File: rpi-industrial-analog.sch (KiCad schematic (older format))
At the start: 68 parts, among them J101 CONN_01X04, J102 CONN_01X08, U101 MCP3424, U102 ICL7660S,A, U103 AD8220, U104 AD8220, U105 AD8220, U106 AD8220

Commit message: Layout complete
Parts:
- added LG101: 3ML_LOGO, 3ML_Footprint_Library:3ML_LOGO, symbol 3ML_LOGO
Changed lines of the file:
@@
+	1    0    0    -1
+$EndComp
+$Comp
+L 3ML_LOGO LG101
+U 1 1 58D9BA61
+P 10800 4450
+F 0 "LG101" H 10810 4590 60  0001 C CNN
+F 1 "3ML_LOGO" H 10800 4310 60  0001 C CNN
+F 2 "3ML_Footprint_Library:3ML_LOGO" H 10800 4450 60  0001 C CNN
+F 3 "X" H 10800 4450 60  0001 C CNN
+F 4 "X" H 10800 4450 60  0001 C CNN "MPN"
+F 5 "X" H 10800 4450 60  0001 C CNN "MFN"
+F 6 "X" H 10800 4450 60  0001 C CNN "Characteristics"
+F 7 "X" H 10800 4450 60  0001 C CNN "Description"
+F 8 "X" H 10800 4450 60  0001 C CNN "Package ID"
+F 9 "X" H 10800 4450 60  0001 C CNN "Source"
+F 10 "Y" H 10800 4450 60  0001 C CNN "Critical"
+F 11 "X" H 10800 4450 60  0001 C CNN "Notes"
+	1    10800 4450
 	1    0    0    -1
 $EndComp

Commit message: adding logos and mounting holes
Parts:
- added ACC101, ACC103, ACC104, ACC105: ACC_?, Mounting_Holes:MountingHole_3.2mm_M3_DIN965, symbol ACC_?
- added ACC102: ACC_?, Symbols:OSHW-Logo_5.7x6mm_SilkScreen, symbol ACC_?
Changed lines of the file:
@@
+	1    0    0    -1
+$EndComp
+$Comp
+L ACC_? ACC101
+U 1 1 58D9BFB7
+P 10800 4800
+F 0 "ACC101" H 10810 4940 60  0000 C CNN
+F 1 "ACC_?" H 10800 4660 60  0000 C CNN
+F 2 "Mounting_Holes:MountingHole_3.2mm_M3_DIN965" H 10800 4800 60  0001 C CNN
+F 3 "X" H 10800 4800 60  0001 C CNN
+F 4 "X" H 10800 4800 60  0001 C CNN "MPN"
+F 5 "X" H 10800 4800 60  0001 C CNN "MFN"
+F 6 "X" H 10800 4800 60  0001 C CNN "Characteristics"
+F 7 "Mounting Hole M3" H 10800 4800 60  0001 C CNN "Description"
+F 8 "X" H 10800 4800 60  0001 C CNN "Package ID"
+F 9 "X" H 10800 4800 60  0001 C CNN "Source"
+F 10 "Y" H 10800 4800 60  0001 C CNN "Critical"
+F 11 "X" H 10800 4800 60  0001 C CNN "Notes"
+	1    10800 4800
+	1    0    0    -1
+$EndComp
+$Comp
+L ACC_? ACC103
+U 1 1 58D9C882
+P 11150 4800
+F 0 "ACC103" H 11160 4940 60  0000 C CNN
+F 1 "ACC_?" H 11150 4660 60  0000 C CNN
+F 2 "Mounting_Holes:MountingHole_3.2mm_M3_DIN965" H 11150 4800 60  0001 C CNN
+F 3 "X" H 11150 4800 60  0001 C CNN
+F 4 "X" H 11150 4800 60  0001 C CNN "MPN"
+F 5 "X" H 11150 4800 60  0001 C CNN "MFN"
+F 6 "X" H 11150 4800 60  0001 C CNN "Characteristics"
+F 7 "Mounting Hole M3" H 11150 4800 60  0001 C CNN "Description"
+F 8 "X" H 11150 4800 60  0001 C CNN "Package ID"
+F 9 "X" H 11150 4800 60  0001 C CNN "Source"
+F 10 "Y" H 11150 4800 60  0001 C CNN "Critical"
+F 11 "X" H 11150 4800 60  0001 C CNN "Notes"
+	1    11150 4800
+	1    0    0    -1
+$EndComp
+$Comp
+L ACC_? ACC104
+U 1 1 58D9C980
+P 11500 4800
+F 0 "ACC104" H 11510 4940 60  0000 C CNN
+F 1 "ACC_?" H 11500 4660 60  0000 C CNN
+F 2 "Mounting_Holes:MountingHole_3.2mm_M3_DIN965" H 11500 4800 60  0001 C CNN
+F 3 "X" H 11500 4800 60  0001 C CNN
+F 4 "X" H 11500 4800 60  0001 C CNN "MPN"
+F 5 "X" H 11500 4800 60  0001 C CNN "MFN"
+F 6 "X" H 11500 4800 60  0001 C CNN "Characteristics"
+F 7 "Mounting Hole M3" H 11500 4800 60  0001 C CNN "Description"
+F 8 "X" H 11500 4800 60  0001 C CNN "Package ID"
+F 9 "X" H 11500 4800 60  0001 C CNN "Source"
+F 10 "Y" H 11500 4800 60  0001 C CNN "Critical"
+F 11 "X" H 11500 4800 60  0001 C CNN "Notes"
+	1    11500 4800
+	1    0    0    -1
+$EndComp
+$Comp
+L ACC_? ACC105
+U 1 1 58D9CA7D
+P 11850 4800
+F 0 "ACC105" H 11860 4940 60  0000 C CNN
+F 1 "ACC_?" H 11850 4660 60  0000 C CNN
+F 2 "Mounting_Holes:MountingHole_3.2mm_M3_DIN965" H 11850 4800 60  0001 C CNN
+F 3 "X" H 11850 4800 60  0001 C CNN
+F 4 "X" H 11850 4800 60  0001 C CNN "MPN"
+F 5 "X" H 11850 4800 60  0001 C CNN "MFN"
+F 6 "X" H 11850 4800 60  0001 C CNN "Characteristics"
+F 7 "Mounting Hole M3" H 11850 4800 60  0001 C CNN "Description"
+F 8 "X" H 11850 4800 60  0001 C CNN "Package ID"
+F 9 "X" H 11850 4800 60  0001 C CNN "Source"
+F 10 "Y" H 11850 4800 60  0001 C CNN "Critical"
+F 11 "X" H 11850 4800 60  0001 C CNN "Notes"
+	1    11850 4800
+	1    0    0    -1
+$EndComp
+$Comp
+L ACC_? ACC102
+U 1 1 58D9CBD3
+P 10800 5250
+F 0 "ACC102" H 10810 5390 60  0000 C CNN
+F 1 "ACC_?" H 10800 5110 60  0000 C CNN
+F 2 "Symbols:OSHW-Logo_5.7x6mm_SilkScreen" H 10800 5250 60  0001 C CNN
+F 3 "X" H 10800 5250 60  0001 C CNN
+F 4 "X" H 10800 5250 60  0001 C CNN "MPN"
+F 5 "X" H 10800 5250 60  0001 C CNN "MFN"
+F 6 "X" H 10800 5250 60  0001 C CNN "Characteristics"
+F 7 "Mounting Hole M3" H 10800 5250 60  0001 C CNN "Description"
+F 8 "X" H 10800 5250 60  0001 C CNN "Package ID"
+F 9 "X" H 10800 5250 60  0001 C CNN "Source"
+F 10 "Y" H 10800 5250 60  0001 C CNN "Critical"
+F 11 "X" H 10800 5250 60  0001 C CNN "Notes"
+	1    10800 5250
 	1    0    0    -1
 $EndComp

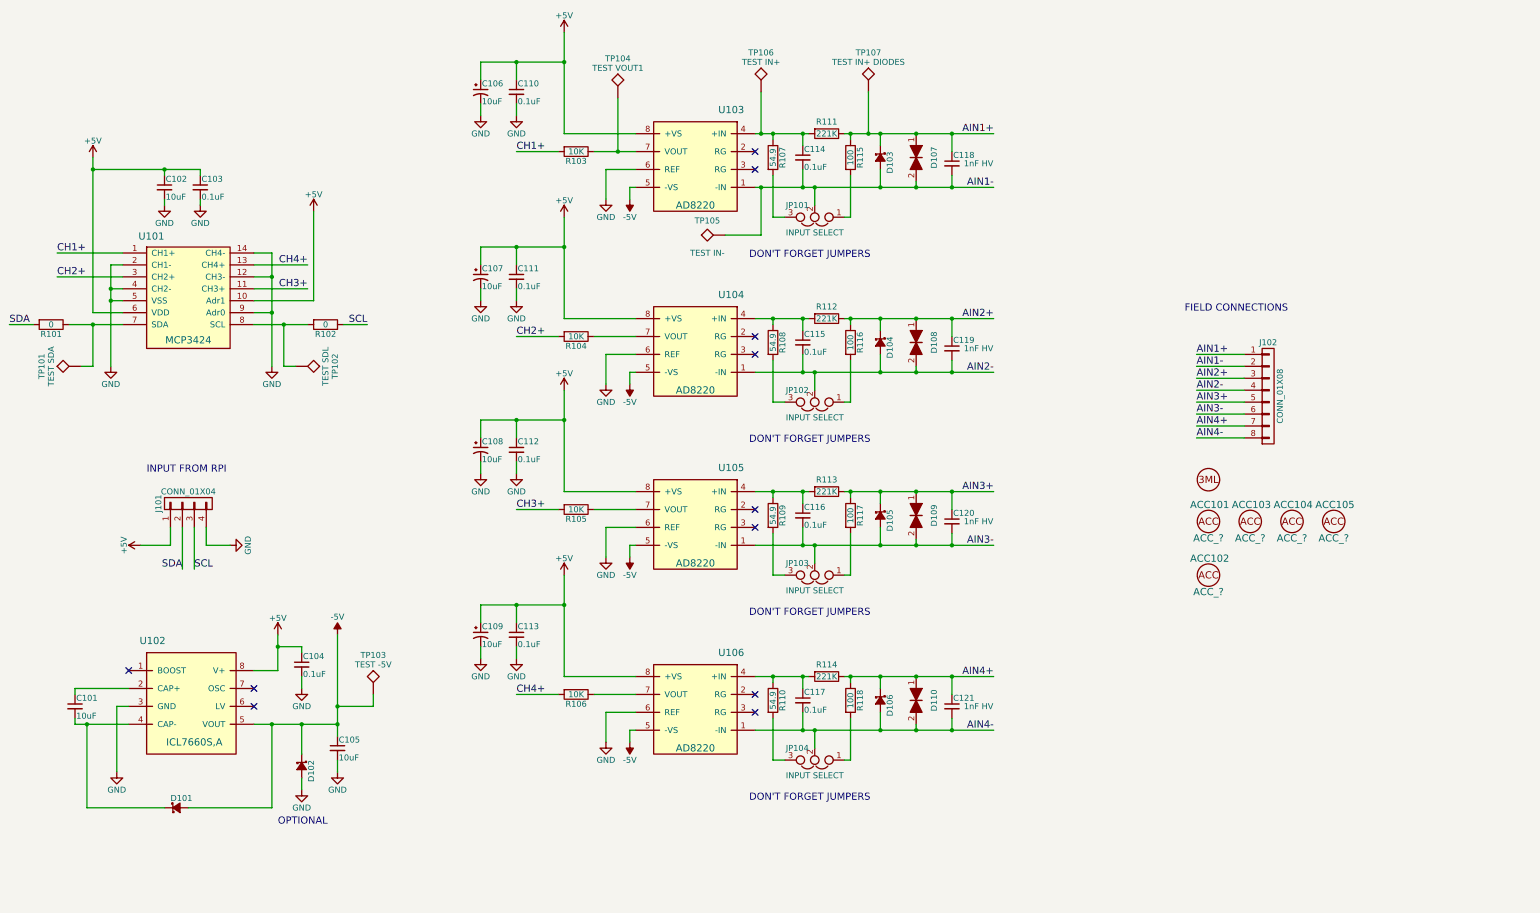
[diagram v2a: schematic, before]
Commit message: revised board for production and added 1M caps so that this thing works
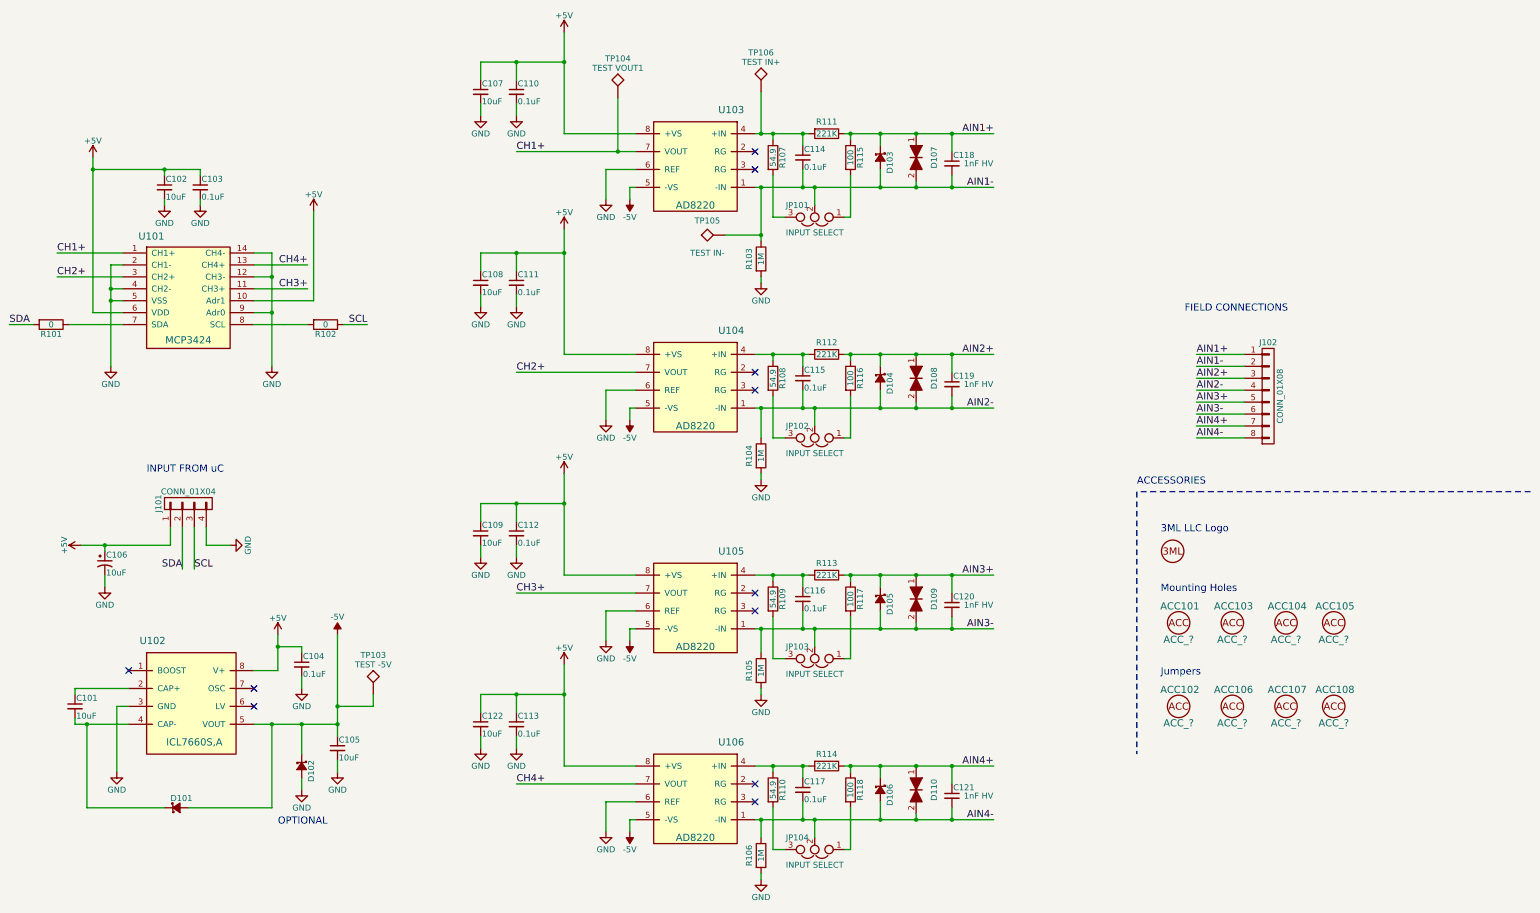
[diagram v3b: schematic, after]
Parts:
- removed C107, C108, C109: 10uF, 3ML_Footprint_Library:C_0805_POL, symbol CP1_Small
- removed TP101: TEST SDA, 3ML_Footprint_Library:Keystone_5000_Test_Point_Mini, symbol TEST
- removed TP102: TEST SDL, 3ML_Footprint_Library:Keystone_5000_Test_Point_Mini, symbol TEST
- removed TP107: TEST IN+ DIODES, 3ML_Footprint_Library:Keystone_5000_Test_Point_Mini, symbol TEST
- added ACC106, ACC107, ACC108: ACC_?, X, symbol ACC_?
- added C107, C108, C109, C122: 10uF, Capacitors_SMD:C_0805, symbol C_Small
- ACC102: footprint Symbols:OSHW-Logo_5.7x6mm_SilkScreen -> X; Description Mounting Hole M3 -> CONN JUMPER SHORTING 1.27MM GOLD; MFN X -> Sullins Connector Solutions; MPN X -> NPB02SVAN-RC; Populate (none) -> 1; Source X -> Digikey
- C106: footprint 3ML_Footprint_Library:C_0805_POL -> Capacitors_Tantalum_SMD:CP_Tantalum_Case-A_EIA-3216-18_Reflow; Description CAP TANT POLY 10UF 10V SMD -> F931A106KAA; MPN F381A106MMAAH1 -> (none); Package ID 0805 -> 1206 (3216 Metric); Populate (none) -> 1
- R103, R104, R105, R106: value 10K -> 1M; Characteristics X -> Value; Description RES SMD 10K OHM 1% 1/4W 0805 -> Value; MFN Stackpole Electronics -> Value; MPN RNCP0805FTD10K0 -> (none); Package ID 0805 -> Value; Populate (none) -> 1
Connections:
- net +5V: now also C107.1, C108.1, C109.1, C122.1
- net AIN1-: now also R103.1
- net AIN2-: now also R104.1
- net AIN3-: now also R105.1
- net AIN4-: now also R106.1
- net CH1+: now also TP104.1, U103.7 (VOUT); no longer R103.2
- net CH2+: now also U104.7 (VOUT); no longer R104.2
- net CH3+: now also U105.7 (VOUT); no longer R105.2
- net CH4+: now also U106.7 (VOUT); no longer R106.2
- net GND: now also R103.2, R104.2, R105.2, R106.2, C107.2, C108.2, C109.2, C122.2
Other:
- note added: "3ML LLC Logo"
- note added: "ACCESSORIES"
- note added: "INPUT FROM uC"
- note added: "Jumpers"
- note added: "Mounting Holes"
- note removed: "DON'T FORGET JUMPERS"
- note removed: "INPUT FROM RPI"
- moved on the sheet: ACC101, ACC103, ACC104, ACC105, C111, C112, C113, C115, C116, C117, C119, C120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

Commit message: adding gerbers, fixing DRC, adding overvoltage diodes to MCP inputs
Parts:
- added D111, D112, D113, D114: D_Schottky_Small_ALT, Diodes_SMD:D_SOD-323, symbol D_Schottky_Small_ALT
- J101: MFN Value -> Harwin; MPN Value -> M20-9990445; Populate (none) -> 1
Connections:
- net +5V: now also D111.1 (K), D112.1 (K), D112.2 (A), D113.1 (K), D113.2 (A), D114.1 (K), D114.2 (A)
- net CH1+: now also D111.2 (A)

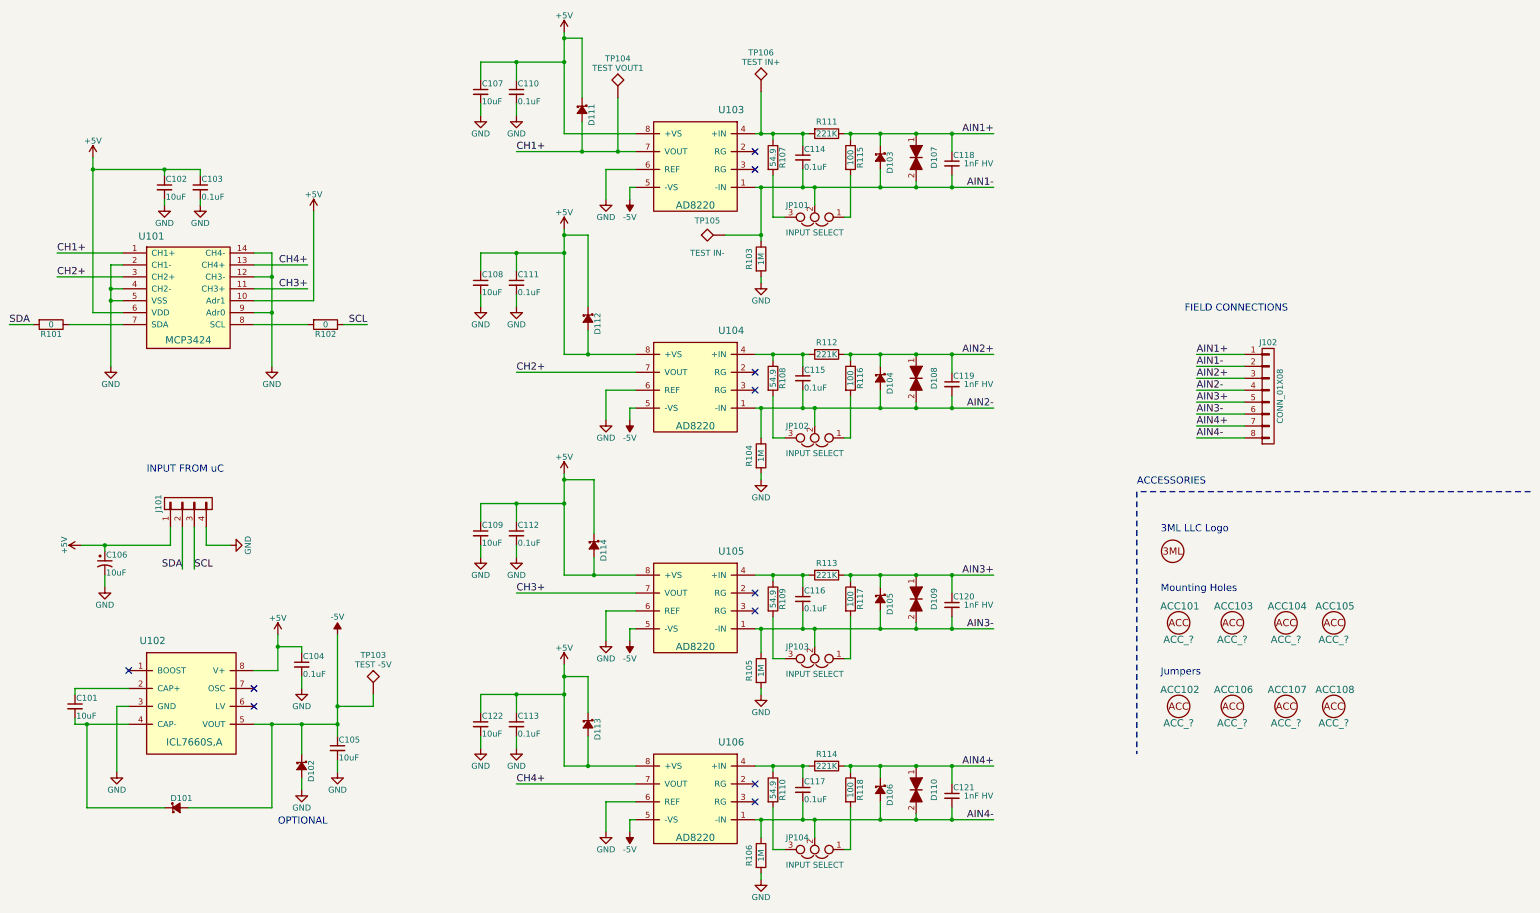
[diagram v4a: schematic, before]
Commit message: cleaning-up Gerbers and step 1 of migrating footprints to master 3ML library
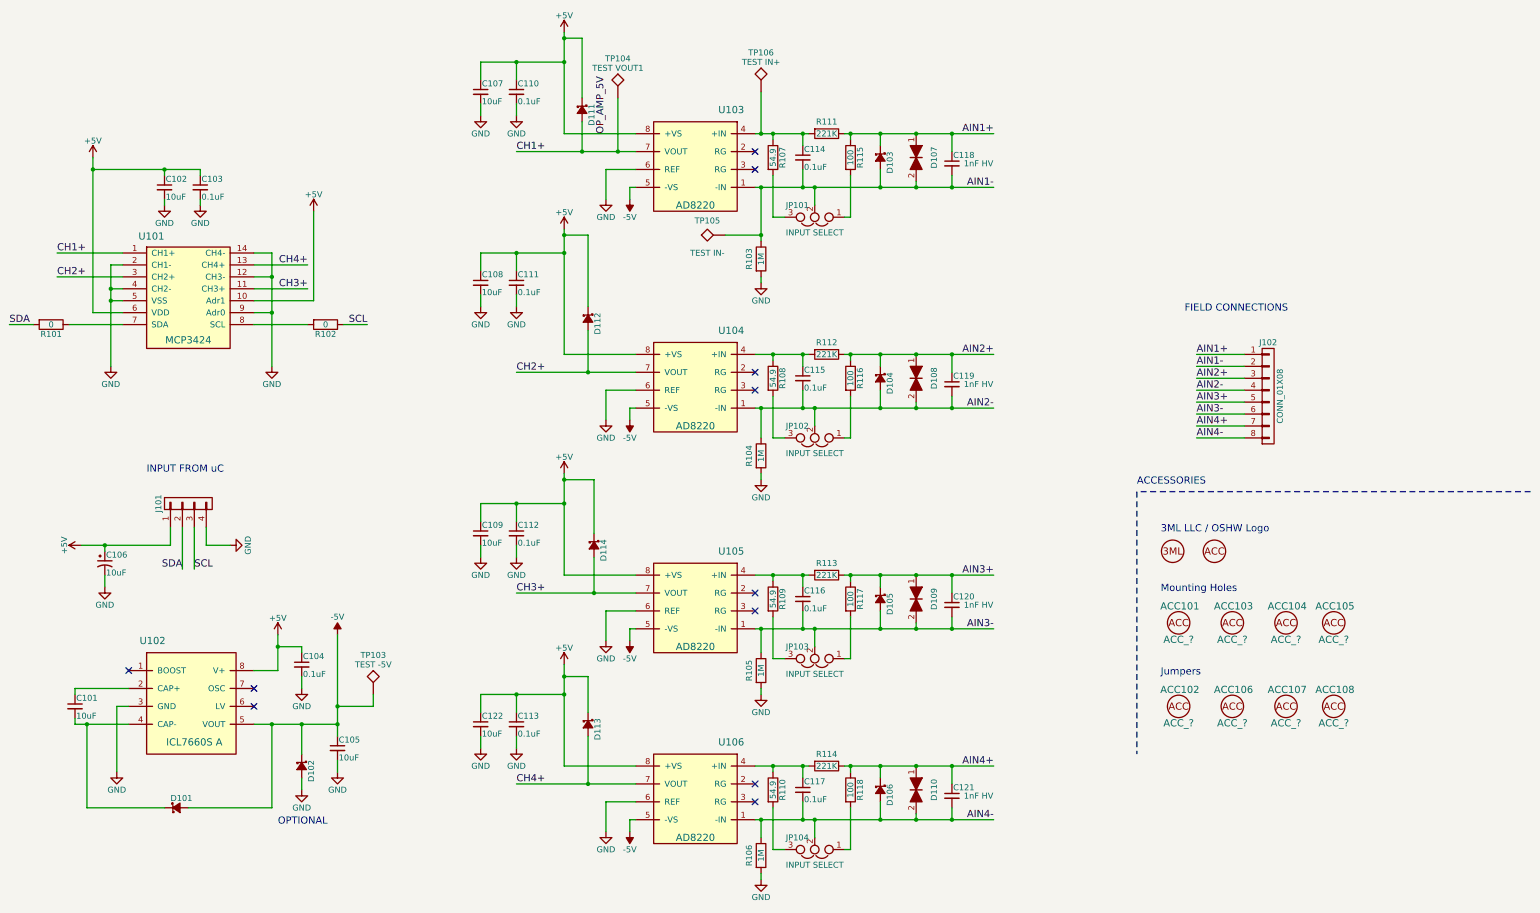
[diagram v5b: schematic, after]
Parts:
- added ACC109: ACC_?, Symbols:OSHW-Logo_11.4x12mm_SilkScreen, symbol ACC_?
- C118, C119, C120, C121: Description 1000pF 250V Ceramic Capacitor X7R 0805 -> CAP CER 1000PF 1KV X7R 0805; MFN Samsung Electro-Mechanics America Inc. -> Johanson Dielectrics Inc.; MPN CL21B102KECSNNC -> 102R15W102KV4E; Populate (none) -> 1
- R103, R104, R105, R106: Characteristics Value -> X; Description Value -> RES SMD 1M OHM 5% 1/8W 0805; MFN Value -> Stackpole Electronics Inc.; MPN (none) -> RMCF0805JT1M00; Package ID Value -> 0805
- U102: value ICL7660S,A -> ICL7660S A; Populate (none) -> 1
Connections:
- net +5V: no longer D112.2 (A), D113.2 (A), D114.2 (A)
- net CH2+: now also D112.2 (A)
- net CH3+: now also D114.2 (A)
- net CH4+: now also D113.2 (A)
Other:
- note added: "3ML LLC / OSHW Logo"
- note removed: "3ML LLC Logo"
